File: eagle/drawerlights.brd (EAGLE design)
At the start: 48.3 x 40.6 mm, 16 parts

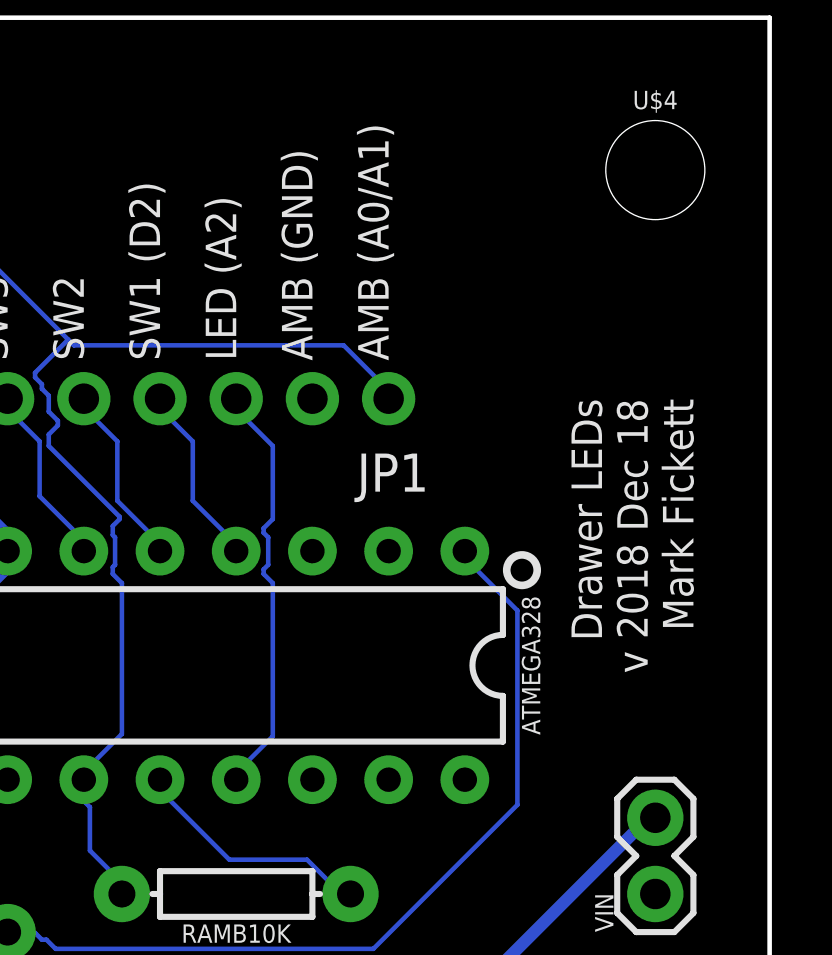
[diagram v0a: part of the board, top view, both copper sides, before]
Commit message: add missing resistor for LED control
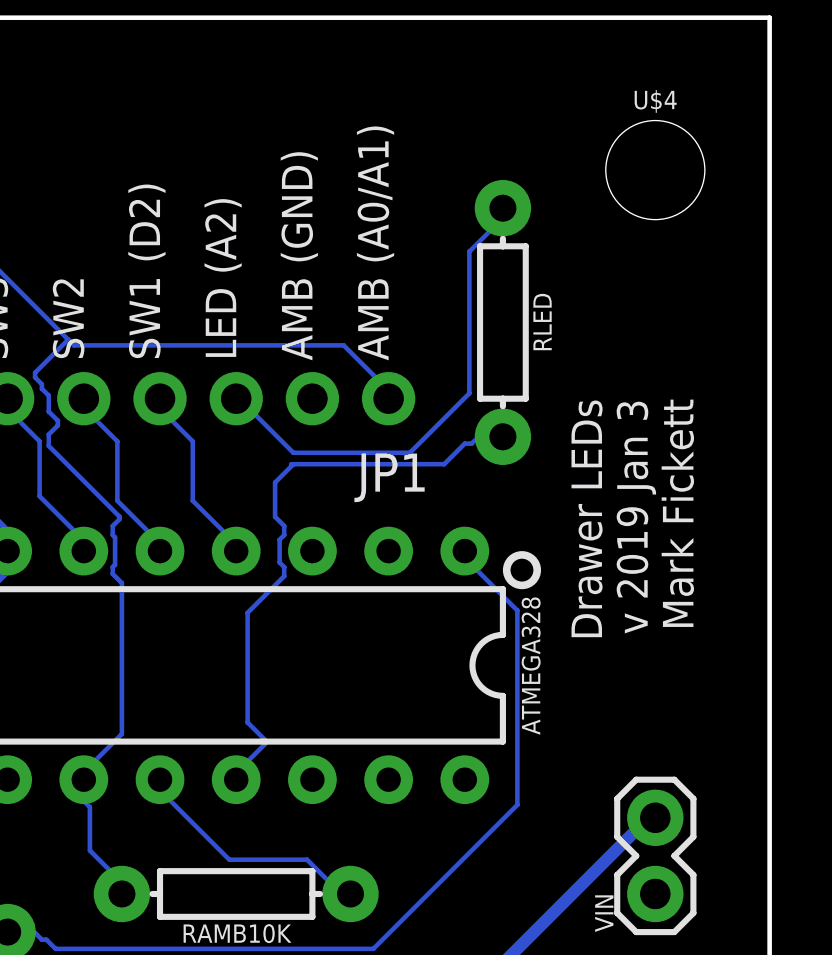
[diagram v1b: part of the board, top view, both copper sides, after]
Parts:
- added RLED: 300-500, SparkFun-Resistors:AXIAL-0.3
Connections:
- new net N$1: JP1.3, RLED.P$1
- net A2LED: now also RLED.P$2; no longer JP1.3
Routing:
- net N$1: track 0.00 -> 16.0 mm
- net A2LED: track 14.1 -> 19.7 mm
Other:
- board text added: "Drawer LEDs v 2019 Jan 3 Mark Fickett"
- board text removed: "Drawer LEDs v 2018 Dec 18 Mark Fickett"
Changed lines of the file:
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@@
 DIV</text>
 <text x="45.72" y="27.94" size="1.016" layer="25" font="fixed" rot="R90" align="bottom-right">Drawer LEDs
-v 2018 Dec 18
+v 2019 Jan 3
 Mark Fickett</text>
 </plain>
@@
 <attribute name="PROD_ID" value="CAP-08439" x="34.29" y="5.08" size="1.778" layer="27" rot="R270" display="off"/>
 </element>
+<element name="RLED" library="SparkFun-Resistors" package="AXIAL-0.3" value="300-500" x="39.37" y="30.48" rot="R270">
+<attribute name="PROD_ID" value="RES-8371" x="39.37" y="30.48" size="1.778" layer="27" rot="R270" display="off"/>
+</element>
 </elements>
 <signals>
@@
 <signal name="A2LED">
 <contactref element="ATMEGA328" pad="25"/>
-<contactref element="JP1" pad="3"/>
 <wire x1="30.48" y1="15.4686" x2="30.48" y2="15.24" width="0.1524" layer="16"/>
-<wire x1="31.6992" y1="16.6878" x2="30.48" y2="15.4686" width="0.1524" layer="16"/>
-<wire x1="31.6992" y1="21.7932" x2="31.6992" y2="16.6878" width="0.1524" layer="16"/>
-<wire x1="31.3944" y1="22.098" x2="31.6992" y2="21.7932" width="0.1524" layer="16"/>
-<wire x1="31.3944" y1="22.2504" x2="31.3944" y2="22.098" width="0.1524" layer="16"/>
-<wire x1="31.5468" y1="22.4028" x2="31.3944" y2="22.2504" width="0.1524" layer="16"/>
-<wire x1="31.5468" y1="23.3172" x2="31.5468" y2="22.4028" width="0.1524" layer="16"/>
-<wire x1="31.3944" y1="23.4696" x2="31.5468" y2="23.3172" width="0.1524" layer="16"/>
-<wire x1="31.3944" y1="23.622" x2="31.3944" y2="23.4696" width="0.1524" layer="16"/>
-<wire x1="31.6992" y1="23.9268" x2="31.3944" y2="23.622" width="0.1524" layer="16"/>
-<wire x1="31.6992" y1="26.3652" x2="31.6992" y2="23.9268" width="0.1524" layer="16"/>
-<wire x1="30.48" y1="27.5844" x2="31.6992" y2="26.3652" width="0.1524" layer="16"/>
-<wire x1="30.48" y1="27.94" x2="30.48" y2="27.5844" width="0.1524" layer="16"/>
+<wire x1="31.5087" y1="16.4973" x2="30.48" y2="15.4686" width="0.1524" layer="16"/>
+<contactref element="RLED" pad="P$2"/>
+<wire x1="37.4142" y1="25.7556" x2="32.385" y2="25.7556" width="0.1524" layer="16"/>
+<wire x1="32.385" y1="25.7556" x2="32.3088" y2="25.7556" width="0.1524" layer="16"/>
+<wire x1="38.1" y1="26.4414" x2="37.4142" y2="25.7556" width="0.1524" layer="16"/>
+<wire x1="38.3286" y1="26.4414" x2="38.1" y2="26.4414" width="0.1524" layer="16"/>
+<wire x1="38.5572" y1="26.67" x2="38.3286" y2="26.4414" width="0.1524" layer="16"/>
+<wire x1="39.37" y1="26.67" x2="38.5572" y2="26.67" width="0.1524" layer="16"/>
+<wire x1="30.861" y1="17.145" x2="31.5087" y2="16.4973" width="0.1524" layer="16"/>
+<wire x1="30.861" y1="20.8026" x2="30.861" y2="17.145" width="0.1524" layer="16"/>
+<wire x1="32.0802" y1="22.0218" x2="30.861" y2="20.8026" width="0.1524" layer="16"/>
+<wire x1="32.0802" y1="22.3266" x2="32.0802" y2="22.0218" width="0.1524" layer="16"/>
+<wire x1="31.9278" y1="22.479" x2="32.0802" y2="22.3266" width="0.1524" layer="16"/>
+<wire x1="31.9278" y1="23.241" x2="31.9278" y2="22.479" width="0.1524" layer="16"/>
+<wire x1="32.0802" y1="23.3934" x2="31.9278" y2="23.241" width="0.1524" layer="16"/>
+<wire x1="32.0802" y1="23.6982" x2="32.0802" y2="23.3934" width="0.1524" layer="16"/>
+<wire x1="31.7754" y1="24.003" x2="32.0802" y2="23.6982" width="0.1524" layer="16"/>
+<wire x1="31.7754" y1="25.146" x2="31.7754" y2="24.003" width="0.1524" layer="16"/>
+<wire x1="32.385" y1="25.7556" x2="31.7754" y2="25.146" width="0.1524" layer="16"/>
 </signal>
 <signal name="D2SW1">
@@
 <wire x1="10.1346" y1="27.8892" x2="10.16" y2="27.94" width="0.1524" layer="16"/>
 </signal>
+<signal name="N$1">
+<contactref element="JP1" pad="3"/>
+<contactref element="RLED" pad="P$1"/>
+<wire x1="30.6324" y1="27.8892" x2="30.48" y2="27.8892" width="0.1524" layer="16"/>
+<wire x1="32.385" y1="26.1366" x2="30.6324" y2="27.8892" width="0.1524" layer="16"/>
+<wire x1="36.2712" y1="26.1366" x2="32.385" y2="26.1366" width="0.1524" layer="16"/>
+<wire x1="38.2524" y1="28.1178" x2="36.2712" y2="26.1366" width="0.1524" layer="16"/>
+<wire x1="38.2524" y1="32.8422" x2="38.2524" y2="28.1178" width="0.1524" layer="16"/>
+<wire x1="39.3192" y1="33.909" x2="38.2524" y2="32.8422" width="0.1524" layer="16"/>
+<wire x1="39.3192" y1="34.29" x2="39.3192" y2="33.909" width="0.1524" layer="16"/>
+<wire x1="30.48" y1="27.8892" x2="30.48" y2="27.94" width="0.1524" layer="16"/>
+<wire x1="39.3192" y1="34.29" x2="39.37" y2="34.29" width="0.1524" layer="16"/>
+</signal>
 </signals>

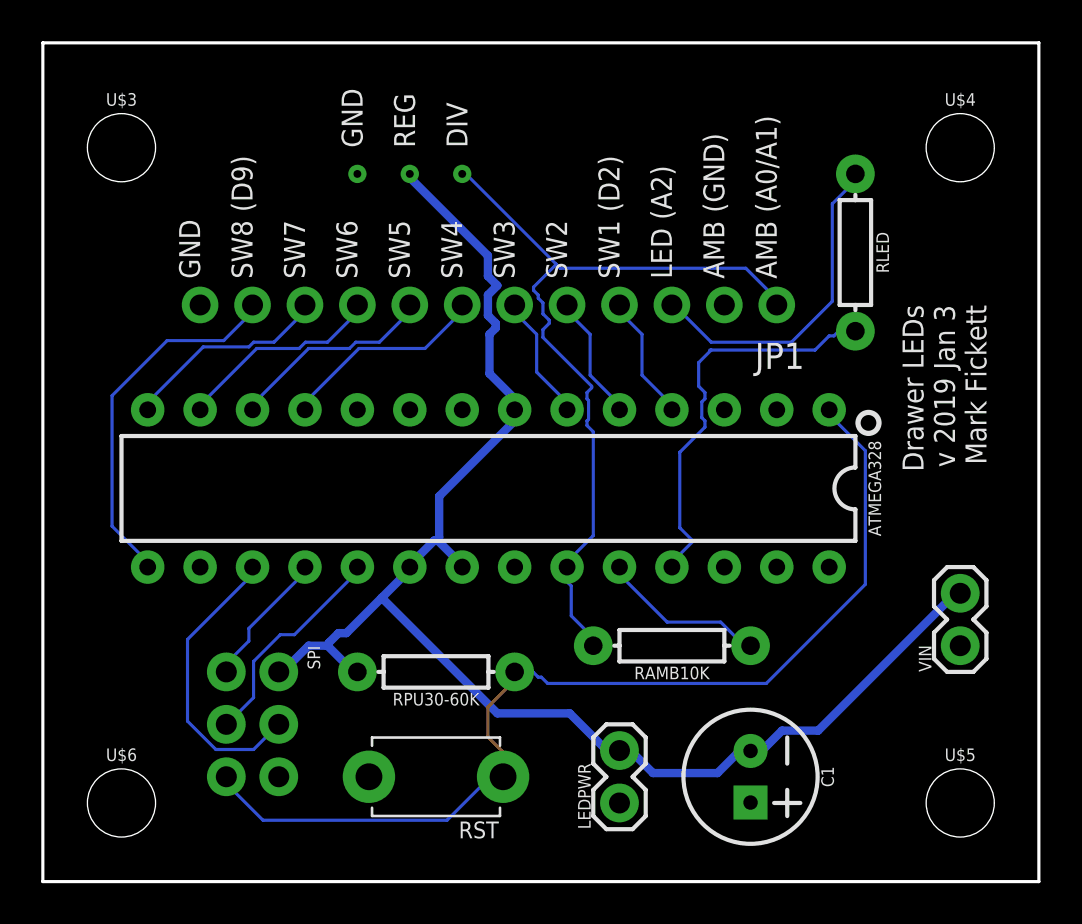
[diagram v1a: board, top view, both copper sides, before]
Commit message: fix vcc and LED power and filter cap polarity
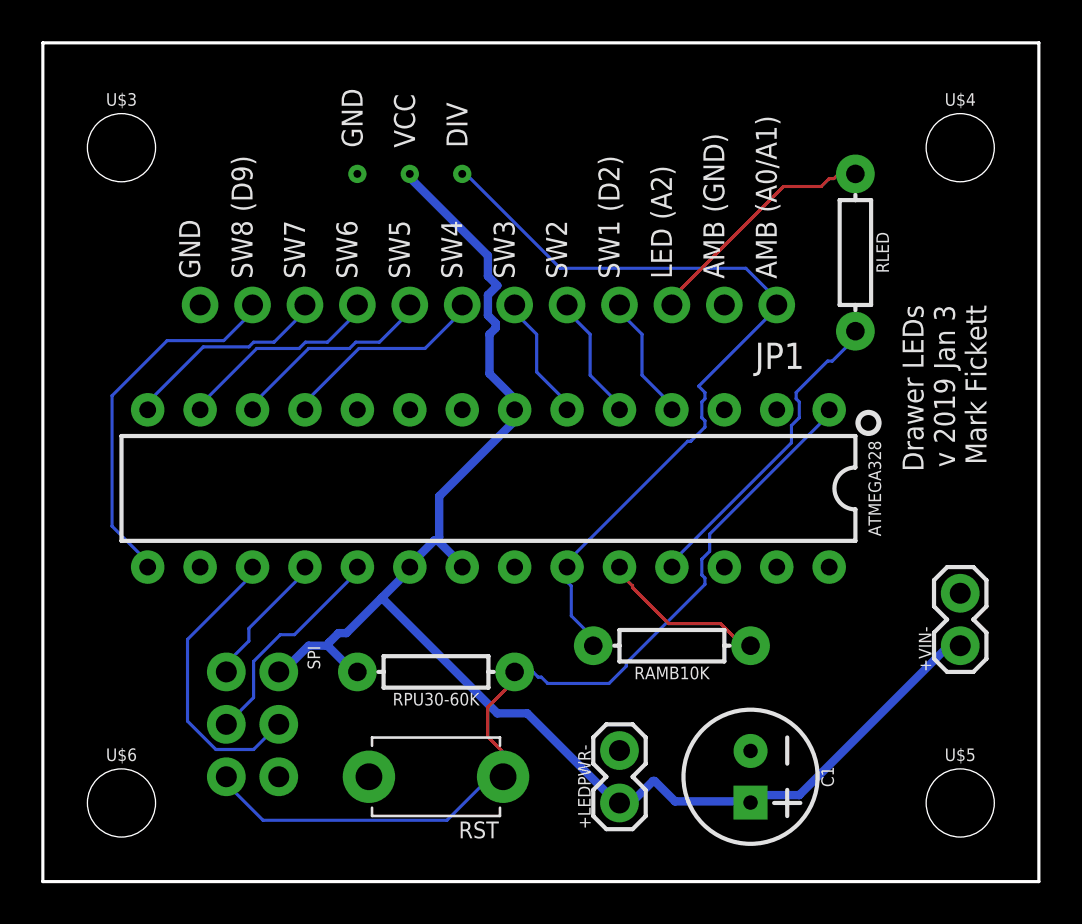
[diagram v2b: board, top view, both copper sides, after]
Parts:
- renumbered LEDPWR to +LEDPWR-, VIN to +VIN-
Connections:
- net GND: now also +LEDPWR-.2, +VIN-.2, C1.2; no longer +LEDPWR-.1, +VIN-.1, C1.1
- net VCCA: now also +LEDPWR-.1, +VIN-.1, C1.1; no longer +LEDPWR-.2, +VIN-.2, C1.2
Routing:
- net RST: track 49.7 -> 43.9 mm
- net N$1: track 16.0 -> 11.7 mm
- net A2LED: track 19.7 -> 15.4 mm
- net VCCA: track 71.6 -> 72.6 mm
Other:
- board text added: "GND VCC DIV"
- board text removed: "GND REG DIV"

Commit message: move LED control to D0, fix # LEDs per drawer 4 => 8
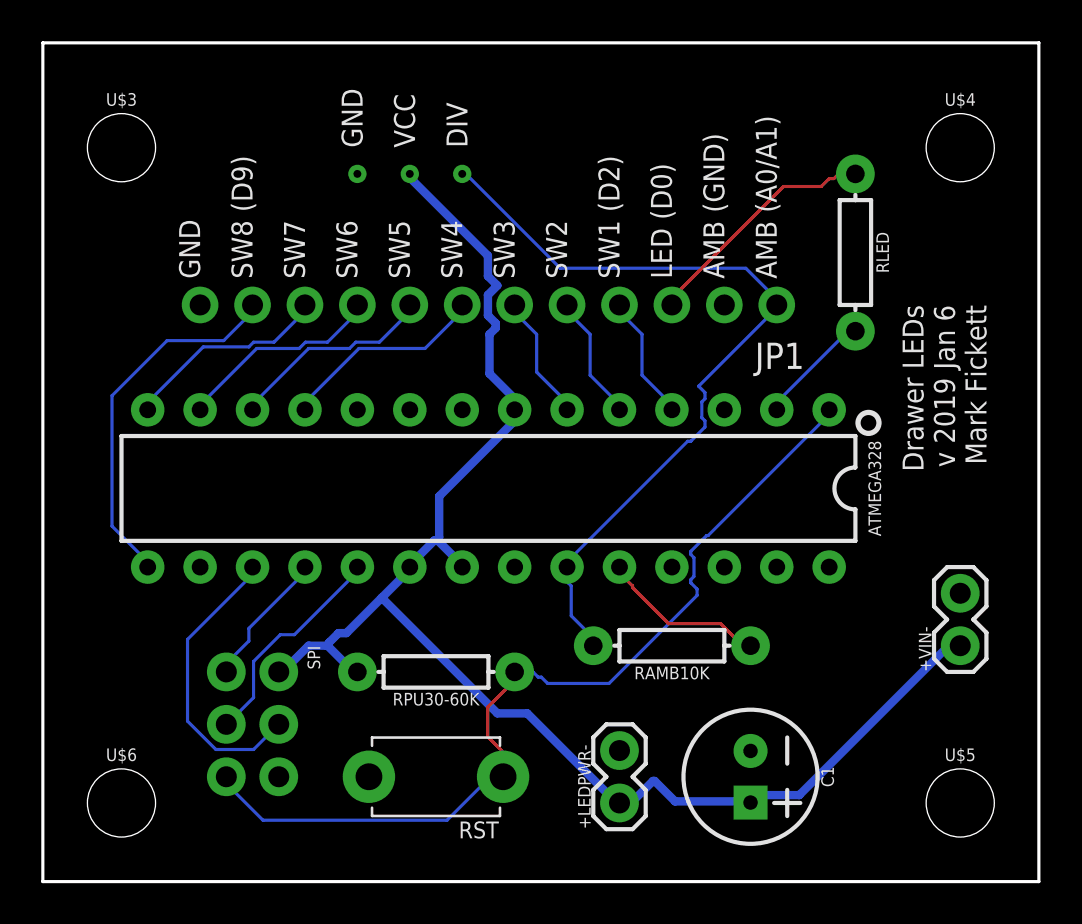
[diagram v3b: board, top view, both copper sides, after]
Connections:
- removed net A2LED: ATMEGA328.25, RLED.P$2
- new net D0LED: ATMEGA328.2, RLED.P$2
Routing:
- net A2LED: track 15.4 -> 0.00 mm
- net D0LED: track 0.00 -> 5.61 mm
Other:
- board text added: "Drawer LEDs v 2019 Jan 6 Mark Fickett"
- board text added: "GND SW8 (D9) SW7 SW6 SW5 SW4 SW3 SW2 SW1 (D2) LED (D0) AMB (GND) AMB (A0/A1)"
- board text removed: "Drawer LEDs v 2019 Jan 3 Mark Fickett"
- board text removed: "GND SW8 (D9) SW7 SW6 SW5 SW4 SW3 SW2 SW1 (D2) LED (A2) AMB (GND) AMB (A0/A1)"
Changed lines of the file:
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@@
 SW2
 SW1 (D2)
-LED (A2)
+LED (D0)
 AMB (GND)
 AMB (A0/A1)</text>
@@
 DIV</text>
 <text x="45.72" y="27.94" size="1.016" layer="25" font="fixed" rot="R90" align="bottom-right">Drawer LEDs
-v 2019 Jan 3
+v 2019 Jan 6
 Mark Fickett</text>
 </plain>
@@
 <wire x1="22.2504" y1="5.0292" x2="22.3" y2="5.08" width="0.1524" layer="16"/>
 <wire x1="38.1" y1="22.6314" x2="38.1" y2="22.86" width="0.1524" layer="16"/>
-<wire x1="32.3088" y1="16.8402" x2="38.1" y2="22.6314" width="0.1524" layer="16"/>
-<wire x1="32.3088" y1="16.002" x2="32.3088" y2="16.8402" width="0.1524" layer="16"/>
-<wire x1="31.9278" y1="15.621" x2="32.3088" y2="16.002" width="0.1524" layer="16"/>
-<wire x1="31.9278" y1="14.859" x2="31.9278" y2="15.621" width="0.1524" layer="16"/>
-<wire x1="32.0802" y1="14.7066" x2="31.9278" y2="14.859" width="0.1524" layer="16"/>
-<wire x1="32.0802" y1="14.4018" x2="32.0802" y2="14.7066" width="0.1524" layer="16"/>
-<wire x1="28.2702" y1="10.5918" x2="32.0802" y2="14.4018" width="0.1524" layer="16"/>
-<wire x1="28.2702" y1="10.4394" x2="28.2702" y2="10.5918" width="0.1524" layer="16"/>
-<wire x1="27.432" y1="9.6012" x2="28.2702" y2="10.4394" width="0.1524" layer="16"/>
+<wire x1="32.2326" y1="16.764" x2="38.1" y2="22.6314" width="0.1524" layer="16"/>
+<wire x1="32.1564" y1="16.764" x2="32.2326" y2="16.764" width="0.1524" layer="16"/>
+<wire x1="31.3944" y1="16.002" x2="32.1564" y2="16.764" width="0.1524" layer="16"/>
+<wire x1="31.3944" y1="15.8496" x2="31.3944" y2="16.002" width="0.1524" layer="16"/>
+<wire x1="31.5468" y1="15.6972" x2="31.3944" y2="15.8496" width="0.1524" layer="16"/>
+<wire x1="31.5468" y1="14.7828" x2="31.5468" y2="15.6972" width="0.1524" layer="16"/>
+<wire x1="31.3944" y1="14.6304" x2="31.5468" y2="14.7828" width="0.1524" layer="16"/>
+<wire x1="31.3944" y1="14.478" x2="31.3944" y2="14.6304" width="0.1524" layer="16"/>
+<wire x1="31.6992" y1="14.1732" x2="31.3944" y2="14.478" width="0.1524" layer="16"/>
+<wire x1="31.6992" y1="13.8684" x2="31.6992" y2="14.1732" width="0.1524" layer="16"/>
+<wire x1="27.432" y1="9.6012" x2="31.6992" y2="13.8684" width="0.1524" layer="16"/>
 <wire x1="24.4602" y1="9.6012" x2="27.432" y2="9.6012" width="0.1524" layer="16"/>
 <wire x1="24.1554" y1="9.906" x2="24.4602" y2="9.6012" width="0.1524" layer="16"/>
@@
 <wire x1="27.9654" y1="15.24" x2="27.94" y2="15.24" width="0.1524" layer="1"/>
 </signal>
-<signal name="A2LED">
-<contactref element="ATMEGA328" pad="25"/>
-<contactref element="RLED" pad="P$2"/>
-<wire x1="30.48" y1="15.4686" x2="30.48" y2="15.24" width="0.1524" layer="16"/>
-<wire x1="36.2712" y1="21.2598" x2="30.48" y2="15.4686" width="0.1524" layer="16"/>
-<wire x1="36.2712" y1="22.098" x2="36.2712" y2="21.2598" width="0.1524" layer="16"/>
-<wire x1="36.6522" y1="22.479" x2="36.2712" y2="22.098" width="0.1524" layer="16"/>
-<wire x1="36.6522" y1="23.241" x2="36.6522" y2="22.479" width="0.1524" layer="16"/>
-<wire x1="36.4998" y1="23.3934" x2="36.6522" y2="23.241" width="0.1524" layer="16"/>
-<wire x1="36.4998" y1="23.6982" x2="36.4998" y2="23.3934" width="0.1524" layer="16"/>
-<wire x1="38.0238" y1="25.2222" x2="36.4998" y2="23.6982" width="0.1524" layer="16"/>
-<wire x1="38.2524" y1="25.2222" x2="38.0238" y2="25.2222" width="0.1524" layer="16"/>
-<wire x1="39.3192" y1="26.289" x2="38.2524" y2="25.2222" width="0.1524" layer="16"/>
-<wire x1="39.3192" y1="26.67" x2="39.3192" y2="26.289" width="0.1524" layer="16"/>
-<wire x1="39.3192" y1="26.67" x2="39.37" y2="26.67" width="0.1524" layer="16"/>
-</signal>
 <signal name="D2SW1">
 <contactref element="ATMEGA328" pad="4"/>
@@
 <wire x1="39.37" y1="34.29" x2="38.5572" y2="34.29" width="0.1524" layer="1"/>
 </signal>
+<signal name="D0LED">
+<contactref element="RLED" pad="P$2"/>
+<contactref element="ATMEGA328" pad="2"/>
+<wire x1="35.5854" y1="23.241" x2="35.5854" y2="22.86" width="0.1524" layer="16"/>
+<wire x1="39.0144" y1="26.67" x2="35.5854" y2="23.241" width="0.1524" layer="16"/>
+<wire x1="39.37" y1="26.67" x2="39.0144" y2="26.67" width="0.1524" layer="16"/>
+<wire x1="35.5854" y1="22.86" x2="35.56" y2="22.86" width="0.1524" layer="16"/>
+</signal>
 </signals>
